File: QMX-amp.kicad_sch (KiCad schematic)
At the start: 2 parts, among them J1 RF-IN, J2 RF-OUT

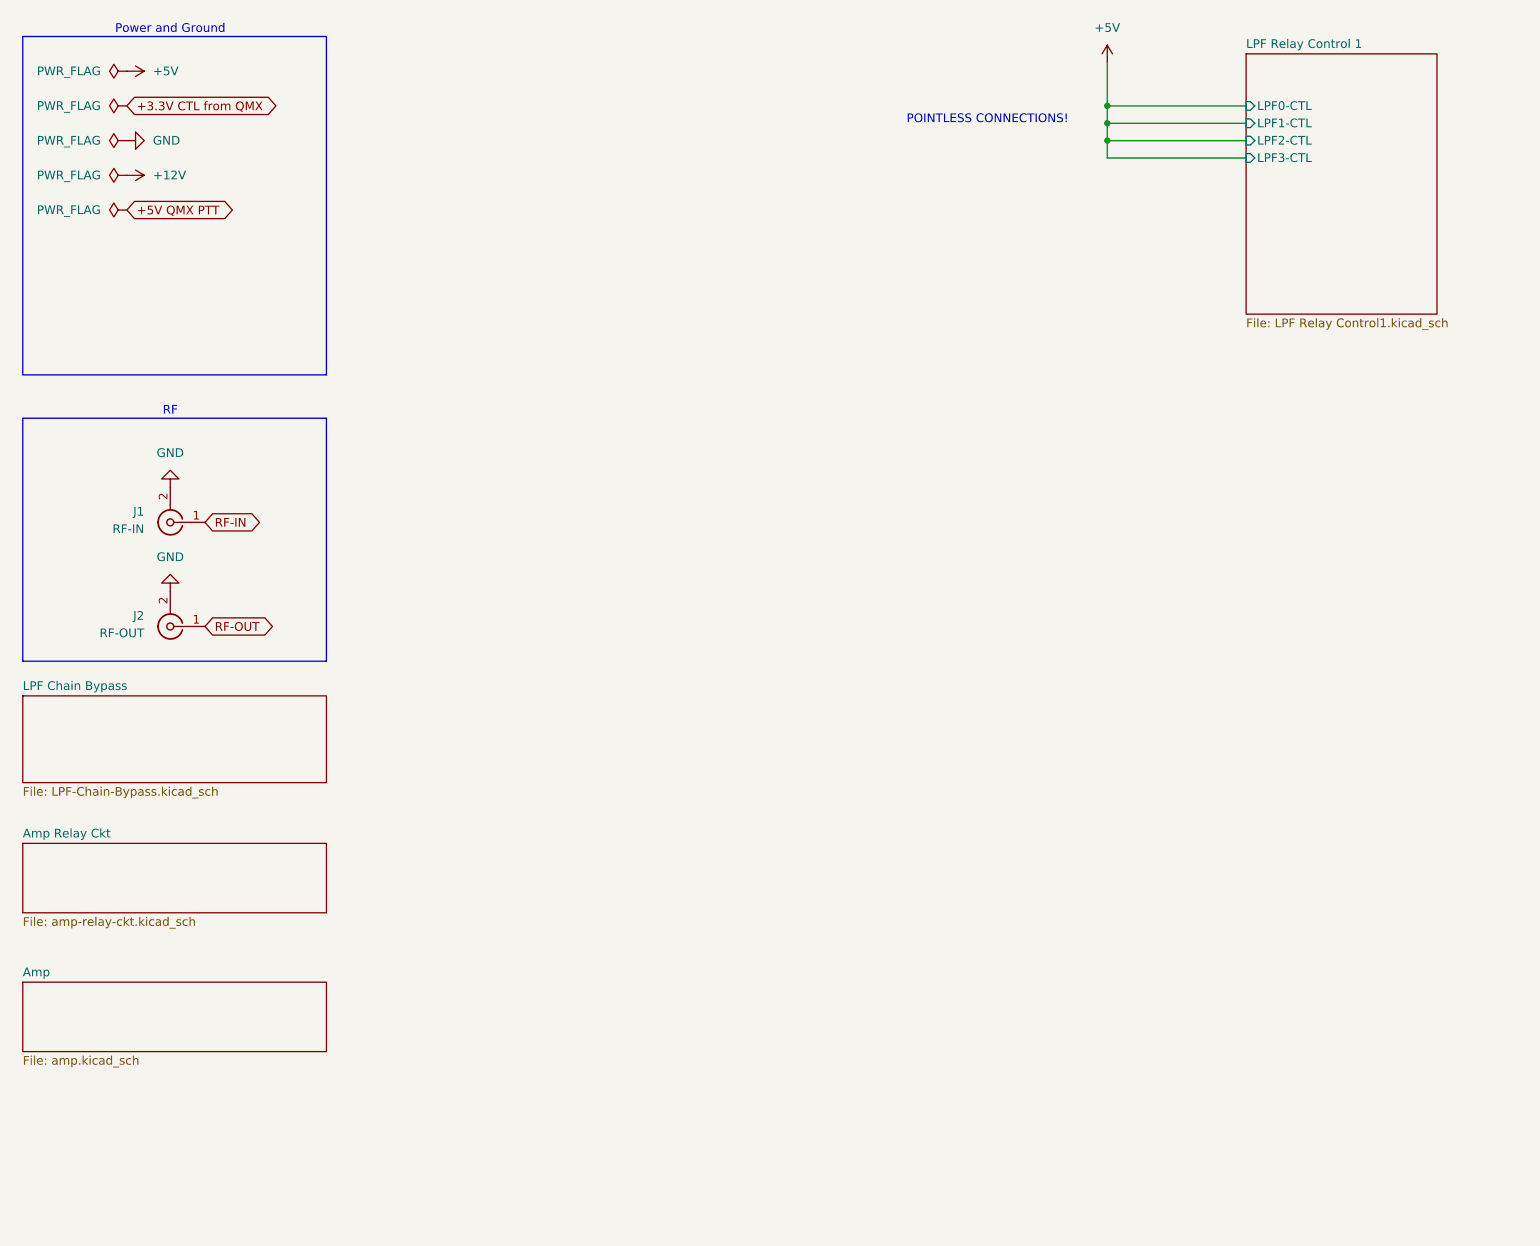
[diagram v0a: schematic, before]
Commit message: v0.6 ERC passes.  I went over it with a fine tooth comb and corrected lots of little stuff.  Ron should review all the components I have to create very carefully.  In particular, MPS-751 symbol does not look correct.
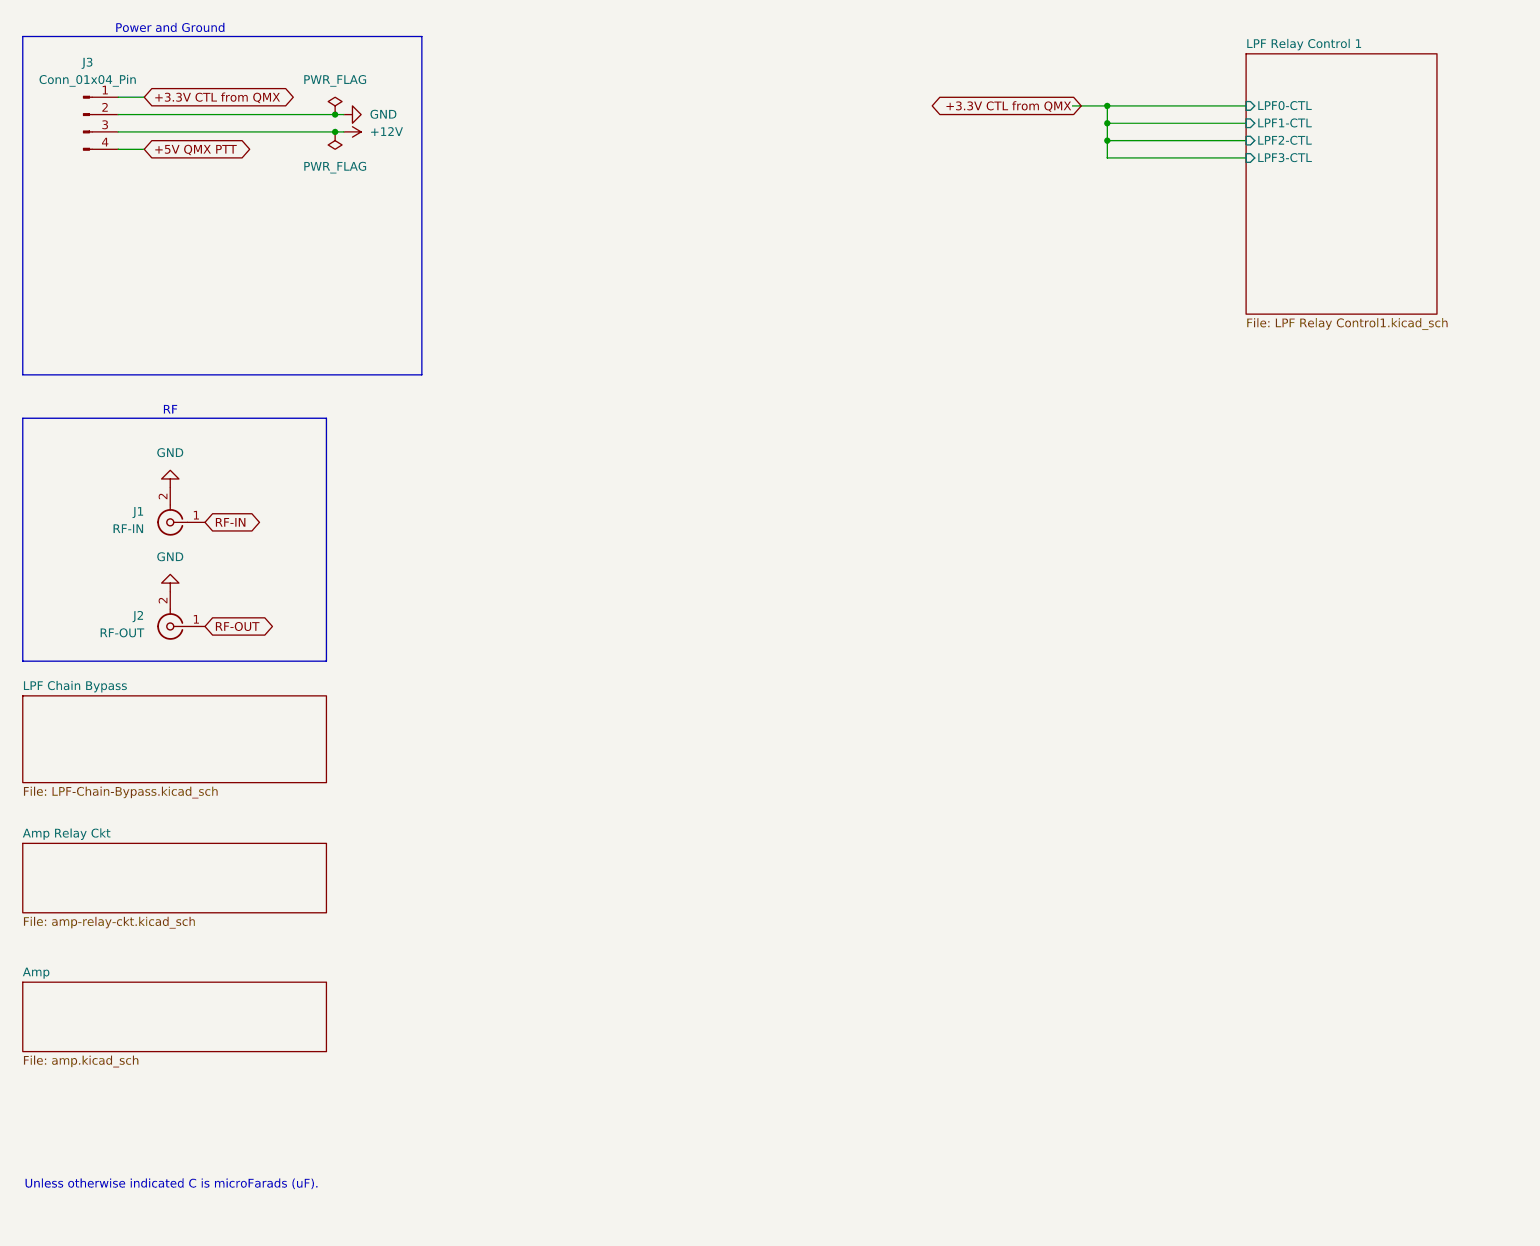
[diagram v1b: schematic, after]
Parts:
- added J3: Conn_01x04_Pin, symbol Connector:Conn_01x04_Pin
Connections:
- net +12V: now also J3.3 (Pin_3)
- net +3.3V CTL from QMX: now also J3.1 (Pin_1)
- net +5V QMX PTT: now also J3.4 (Pin_4)
- net GND: now also J3.2 (Pin_2)
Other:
- note added: "Unless otherwise indicated C is microFarads (uF)."
- note removed: "POINTLESS CONNECTIONS!"
- title: QMX Amp -> QMX+ Amp

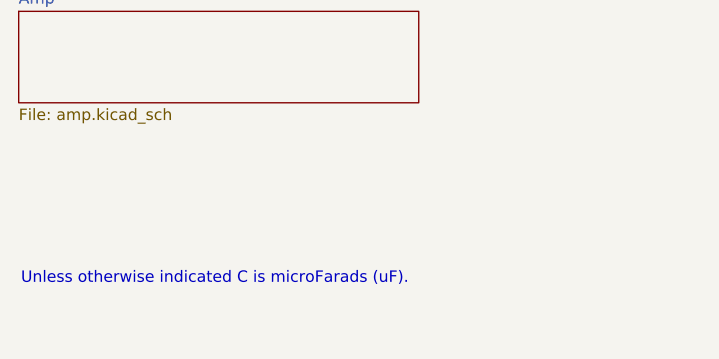
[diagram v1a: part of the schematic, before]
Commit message: v0.7 fixed MPS-751 and bifilar on FT50-43.  ERC passes
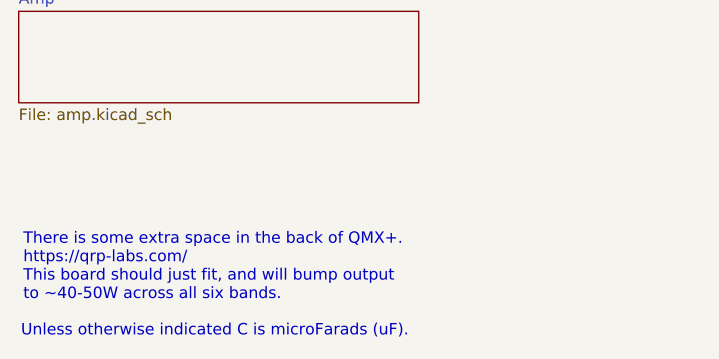
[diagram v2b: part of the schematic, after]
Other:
- note added: "There is some extra space in the back of QMX+. https://qrp-labs.com/ This board should just fit, and will bump output to ~40-50W across all six bands."
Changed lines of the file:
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@@
 		(title "QMX+ Amp")
 		(date "2024-08-13")
-		(rev "v0.6")
+		(rev "v0.7")
 		(company "WA7GIL")
 	)
@@
 	(text "Unless otherwise indicated C is microFarads (uF).\n"
 		(exclude_from_sim no)
-		(at 16.764 191.008 0)
+		(at 16.764 196.85 0)
 		(effects
 			(font
@@
 		)
 	)
+	(text "There is some extra space in the back of QMX+.\nhttps://qrp-labs.com/\nThis board should just fit, and will bump output \nto ~40-50W across all six bands."
+		(exclude_from_sim no)
+		(at 17.018 189.738 0)
+		(effects
+			(font
+				(size 1.27 1.27)
+			)
+			(justify left)
+		)
+	)

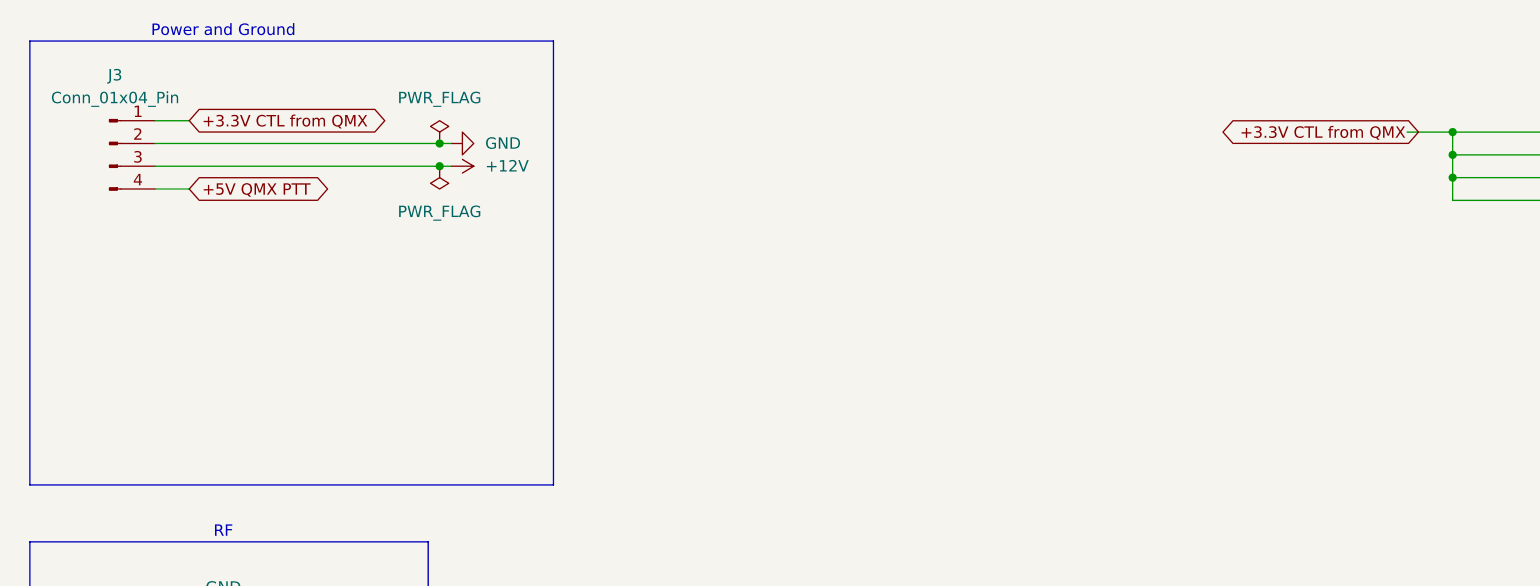
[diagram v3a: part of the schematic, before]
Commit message: ron came by and gave lots of feedback.  many notes on schematic for additional changes
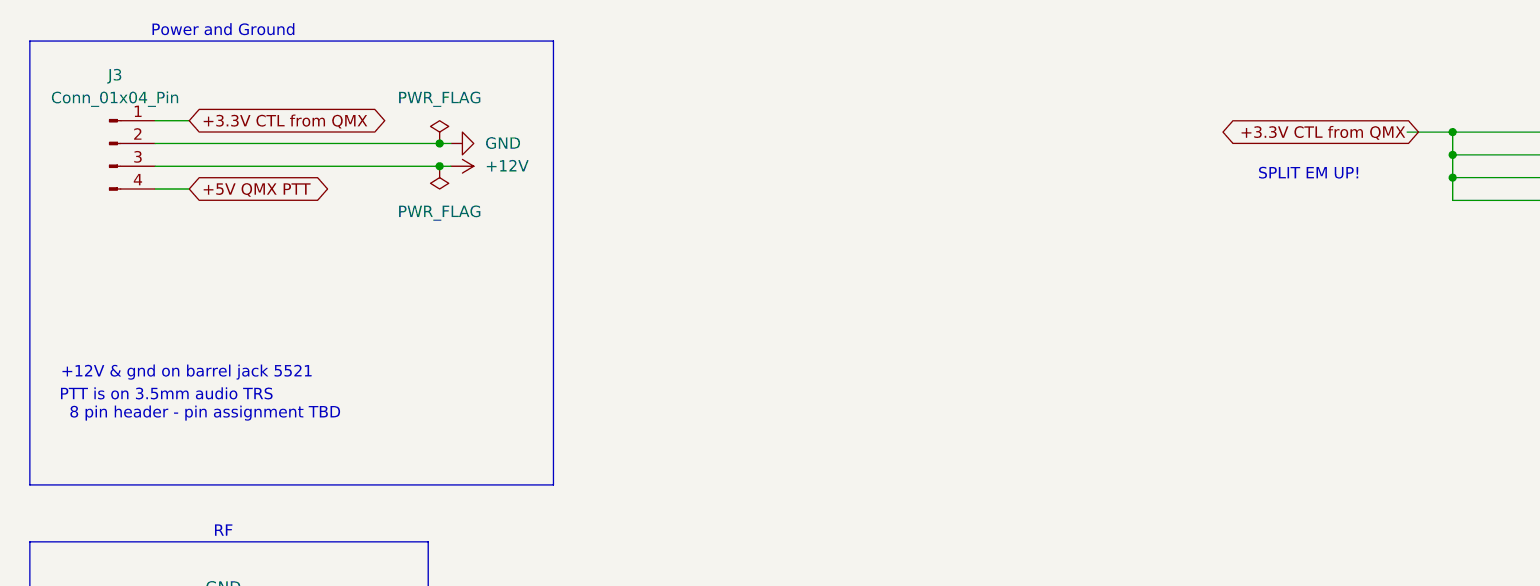
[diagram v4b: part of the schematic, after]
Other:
- note added: "+12V & gnd on barrel jack 5521"
- note added: "8 pin header - pin assignment TBD"
- note added: "PTT is on 3.5mm audio TRS"
- note added: "SPLIT EM UP!"
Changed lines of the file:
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@@
+		)
+	)
+	(text "8 pin header - pin assignment TBD\n"
+		(exclude_from_sim no)
+		(at 36.068 64.516 0)
+		(effects
+			(font
+				(size 1.27 1.27)
+			)
 		)
 	)
@@
 		)
 	)
+	(text "SPLIT EM UP!"
+		(exclude_from_sim no)
+		(at 159.258 37.846 0)
+		(effects
+			(font
+				(size 1.27 1.27)
+			)
+		)
+	)
+	(text "+12V & gnd on barrel jack 5521"
+		(exclude_from_sim no)
+		(at 34.036 59.944 0)
+		(effects
+			(font
+				(size 1.27 1.27)
+			)
+		)
+	)
+	(text "PTT is on 3.5mm audio TRS"
+		(exclude_from_sim no)
+		(at 31.75 62.484 0)
+		(effects
+			(font
+				(size 1.27 1.27)
+			)
+		)
+	)

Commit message: checkpoint changes
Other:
- note added: "now that we have an audio jack selected, place it and wire it in"
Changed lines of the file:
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@@
+		)
+	)
+	(text "now that we have an audio jack selected, place it and wire it in"
+		(exclude_from_sim no)
+		(at 153.162 100.33 0)
+		(effects
+			(font
+				(size 1.27 1.27)
+			)
 		)
 	)

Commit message: v0.8 after much hacking of BS audio footprint from Digikey we now have a 3.5mm audio jack wired in.  ERC pass
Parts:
- added U4: SJ1-3523N, ZZZMyLibrary:SJ1-3523N_CUD, symbol ZZZMyLibrary:SJ1-3523N
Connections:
- net +5V QMX PTT: now also U4.1 (sleeve); no longer J3.4 (Pin_4)
- net GND: now also U4.3 (ring)
- no-connect marks 0 -> 2
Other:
- note added: "3.5mm audio jack tip: NC sleeve: +5V PTT from QMX+ ring: GND"
- note added: "when you get a PCB populated, expand #LPF to full size"
- note removed: "PTT is on 3.5mm audio TRS"
- note removed: "now that we have an audio jack selected, place it and wire it in"
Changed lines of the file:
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@@
 	(title_block
 		(title "QMX+ Amp")
-		(date "2024-08-18")
-		(rev "v0.7")
+		(date "2024-08-19")
+		(rev "v0.8")
 		(company "WA7GIL")
 	)
@@
 		(color 0 0 0 0)
 	)
+	(no_connect
+		(at 30.48 39.37)
+	)
+	(no_connect
+		(at 133.35 121.92)
+	)
 	(wire
 		(pts
@@
 		(pts
 			(xy 195.58 40.64) (xy 175.26 40.64)
-		)
-		(stroke
-			(width 0)
-			(type default)
-		)
-	)
-	(wire
-		(pts
-			(xy 30.48 39.37) (xy 34.29 39.37)
 		)
 		(stroke
@@
 		)
 	)
-	(text "now that we have an audio jack selected, place it and wire it in"
+	(text "when you get a PCB populated, expand #LPF to full size\n"
 		(exclude_from_sim no)
 		(at 153.162 100.33 0)
@@
 		)
 	)
+	(text "3.5mm audio jack\ntip: NC\nsleeve: +5V PTT from QMX+\nring: GND"
+		(exclude_from_sim no)
+		(at 100.838 134.874 0)
+		(effects
+			(font
+				(size 1.27 1.27)
+			)
+			(justify left)
+		)
+	)
 	(text "There is some extra space in the back of QMX+.\nhttps://qrp-labs.com/\nThis board should just fit, and will bump output \nto ~40-50W across all six bands."
 		(exclude_from_sim no)
@@
 		(exclude_from_sim no)
 		(at 34.036 59.944 0)
-		(effects
-			(font
-				(size 1.27 1.27)
-			)
-		)
-	)
-	(text "PTT is on 3.5mm audio TRS"
-		(exclude_from_sim no)
-		(at 31.75 62.484 0)
 		(effects
 			(font
@@
 	(global_label "+5V QMX PTT"
 		(shape bidirectional)
-		(at 34.29 39.37 0)
+		(at 133.35 119.38 0)
 		(fields_autoplaced yes)
 		(effects
@@
 		)
 		(property "Intersheetrefs" "${INTERSHEET_REFS}"
-			(at 51.3886 39.37 0)
+			(at 150.4486 119.38 0)
 			(effects
 				(font
@@
 	)
 	(symbol
+		(lib_id "power:GND")
+		(at 133.35 124.46 90)
+		(unit 1)
+		(exclude_from_sim no)
+		(in_bom yes)
+		(on_board yes)
+		(dnp no)
+		(fields_autoplaced yes)
+		(property "Reference" "#PWR030"
+			(at 139.7 124.46 0)
+			(effects
+				(font
+					(size 1.27 1.27)
+				)
+				(hide yes)
+			)
+		)
+		(property "Value" "GND"
+			(at 137.16 124.4599 90)
+			(effects
+				(font
+					(size 1.27 1.27)
+				)
+				(justify right)
+			)
+		)
+		(property "Footprint" ""
+			(at 133.35 124.46 0)
+			(effects
+				(font
+					(size 1.27 1.27)
+				)
+				(hide yes)
+			)
+		)
+		(property "Datasheet" ""
+			(at 133.35 124.46 0)
+			(effects
+				(font
+					(size 1.27 1.27)
+				)
+				(hide yes)
+			)
+		)
+		(property "Description" "Power symbol creates a global label with name \"GND\" , ground"
+			(at 133.35 124.46 0)
+			(effects
+				(font
+					(size 1.27 1.27)
+				)
+				(hide yes)
+			)
+		)
+		(pin "1"
+		)
+		(instances
+			(project "QMX-amp"
+				(path "/e63e39d7-6ac0-4ffd-8aa3-1841a4541b55"
+					(reference "#PWR030")
+					(unit 1)
+				)
+			)
+		)
+	)
+	(symbol
 		(lib_id "Connector:Conn_01x04_Pin")
 		(at 25.4 34.29 0)
@@
 					(unit 1)
 				)
+			)
+		)
+	)
+	(symbol
+		(lib_id "ZZZMyLibrary:SJ1-3523N")
+		(at 133.35 119.38 0)
+		(mirror y)
+		(unit 1)
+		(exclude_from_sim no)
+		(in_bom yes)
+		(on_board yes)
+		(dnp no)
+		(property "Reference" "U4"
+			(at 113.03 109.22 0)
+			(effects
+				(font
+					(size 1.524 1.524)
+				)
+			)
+		)
+		(property "Value" "SJ1-3523N"
+			(at 113.03 111.76 0)
+			(effects
+				(font
+					(size 1.524 1.524)
+				)
+			)
+		)
+		(property "Footprint" "ZZZMyLibrary:SJ1-3523N_CUD"
+			(at 114.808 104.902 0)
+			(effects
+				(font
+					(size 1.27 1.27)
+					(italic yes)
+				)
+				(hide yes)
+			)
+		)
+		(property "Datasheet" "https://www.cuidevices.com/product/resource/sj1-352xn.pdf"
+			(at 114.808 100.584 0)
+			(effects
+				(font
+					(size 1.27 1.27)
+					(italic yes)
+				)
+				(hide yes)
+			)
+		)
+		(property "Description" ""
+			(at 133.35 119.38 0)
+			(effects
+				(font
+					(size 1.27 1.27)
+				)
+				(hide yes)
+			)
+		)
+		(pin "1"
+		)
+		(pin "3"
+		)
+		(pin "2"
+		)
+		(instances
+			(project ""
+				(path "/e63e39d7-6ac0-4ffd-8aa3-1841a4541b55"
+					(reference "U4")
+					(unit 1)
+				)
